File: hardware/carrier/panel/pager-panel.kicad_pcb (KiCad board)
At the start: 2 copper layers, 40 x 20 mm, 23 parts, among them J1 GDEY029T94 FPC, J2 CARRIER, J3 FRONTLIGHT FPC, Q5 AO3400A

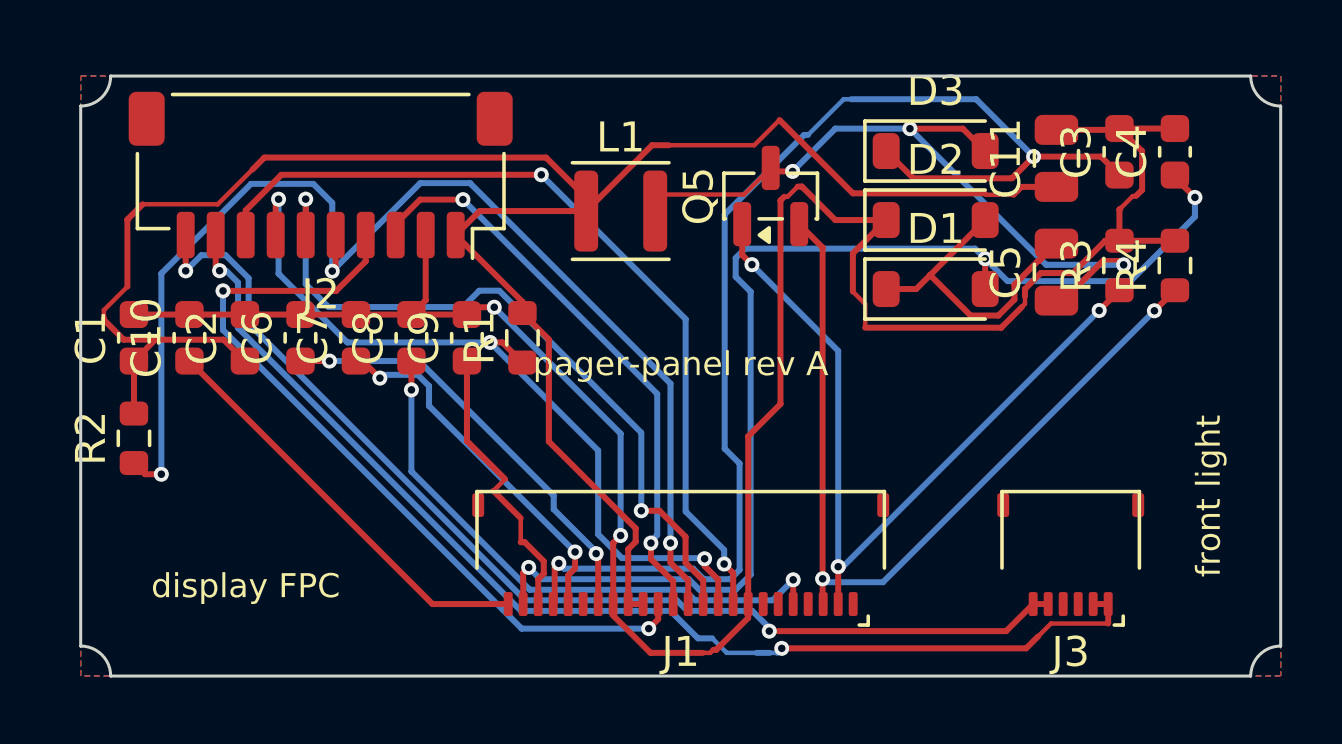
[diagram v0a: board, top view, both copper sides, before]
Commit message: Fix some small errors and clean up BOM
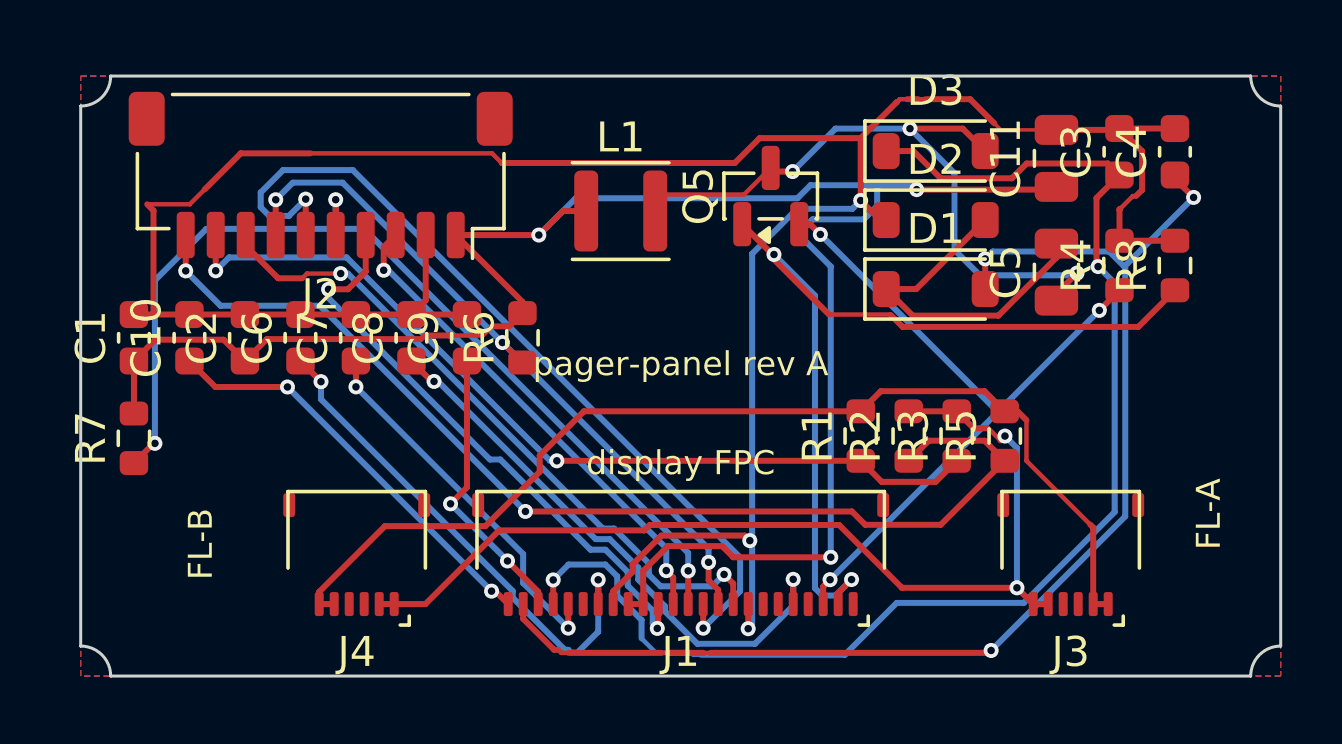
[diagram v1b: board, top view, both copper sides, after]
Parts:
- added J4: FL-B FPC (Orient), pager-carrier:Hirose_FH34SRJ-6S-0.5SH_1x06-1MP_P0.50mm_Horizontal, F.Cu at (9.20, 17.6)
- added R5: 0R, Resistor_SMD:R_0603_1608Metric, F.Cu at (30.8, 12.0)
- added R6: 10k, Resistor_SMD:R_0603_1608Metric, F.Cu at (14.7, 8.72)
- added R7: 10k, Resistor_SMD:R_0603_1608Metric, F.Cu at (1.77, 12.1)
- added R8: 1M, Resistor_SMD:R_0603_1608Metric, F.Cu at (36.5, 6.32)
- J3: value FRONTLIGHT FPC -> FL-A FPC (FL03)
- R1, R2: value 10k -> 0R
- R3: value 1M -> 0R
- moved R2 25.8 mm to (27.6, 12.0)
- moved R1 11.7 mm to (26.0, 12.0)
- moved R3 7.86 mm to (29.2, 12.0)
- moved R4 1.85 mm to (34.6, 6.32)
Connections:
- net EPD_BUSY renamed EINK_BUSY
- net EPD_DC renamed EINK_DC
- net EPD_MOSI renamed EINK_MOSI
- net EPD_SCK renamed EINK_SCK
- J1 pad 10: EPD_RST -> EINK_RST
- J1 pad 12: EPD_CS -> EINK_CS
- J2 pad 10: FL_CATHODE -> FL_N
- J2 pad 5: EPD_CS -> EINK_CS
- J2 pad 7: EPD_RST -> EINK_RST
- J2 pad 9: FL_ANODE -> FL_P
- J3 pad 1: FL_ANODE -> FL_A
- J3 pad 2: FL_ANODE -> FL_A
- J3 pad 5: FL_CATHODE -> FL_K
- J3 pad 6: FL_CATHODE -> FL_K
- R1 pad 1: EPD_RST -> FL_P
- R1 pad 2: 3V3_EPD -> FL_A
- R2 pad 1: EPD_CS -> FL_N
- R2 pad 2: 3V3_EPD -> FL_K
- R3 pad 1: EPD_GDR -> FL_P
- R3 pad 2: GND -> FL_K
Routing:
- net EPD_CS: track 41.3 -> 0.00 mm, vias 3 -> 0
- net FL_ANODE: track 38.6 -> 0.00 mm, vias 2 -> 0
- net FL_CATHODE: track 36.7 -> 0.00 mm, vias 2 -> 0
- net FL_N: track 0.00 -> 36.6 mm, vias 0 -> 2
- net FL_A: track 0.00 -> 35.5 mm
- net FL_K: track 0.00 -> 33.4 mm, vias 0 -> 2
- net EINK_CS: track 0.00 -> 33.2 mm, vias 0 -> 3
- net FL_P: track 0.00 -> 29.5 mm, vias 0 -> 2
- net EPD_RST: track 26.5 -> 0.00 mm, vias 3 -> 0
- net EINK_RST: track 0.00 -> 23.8 mm, vias 0 -> 3
- net GND: track 75.5 -> 87.4 mm, vias 2 -> 3
- net EINK_MOSI: track 26.6 -> 19.9 mm
- net EINK_BUSY: track 28.1 -> 22.6 mm
- net EPD_RESE: track 28.8 -> 23.8 mm, vias 2 -> 3
- net EINK_DC: track 24.6 -> 28.9 mm
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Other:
- board text added: "FL-A"
- board text added: "FL-B"
- board text removed: "front light"
